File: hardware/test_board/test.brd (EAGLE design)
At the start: 70.5 x 75.9 mm, 25 parts, among them IC2 MAX707CPA, IC3 74HCT573N, IC5 7805DT, J2 POWER_JACKSLT

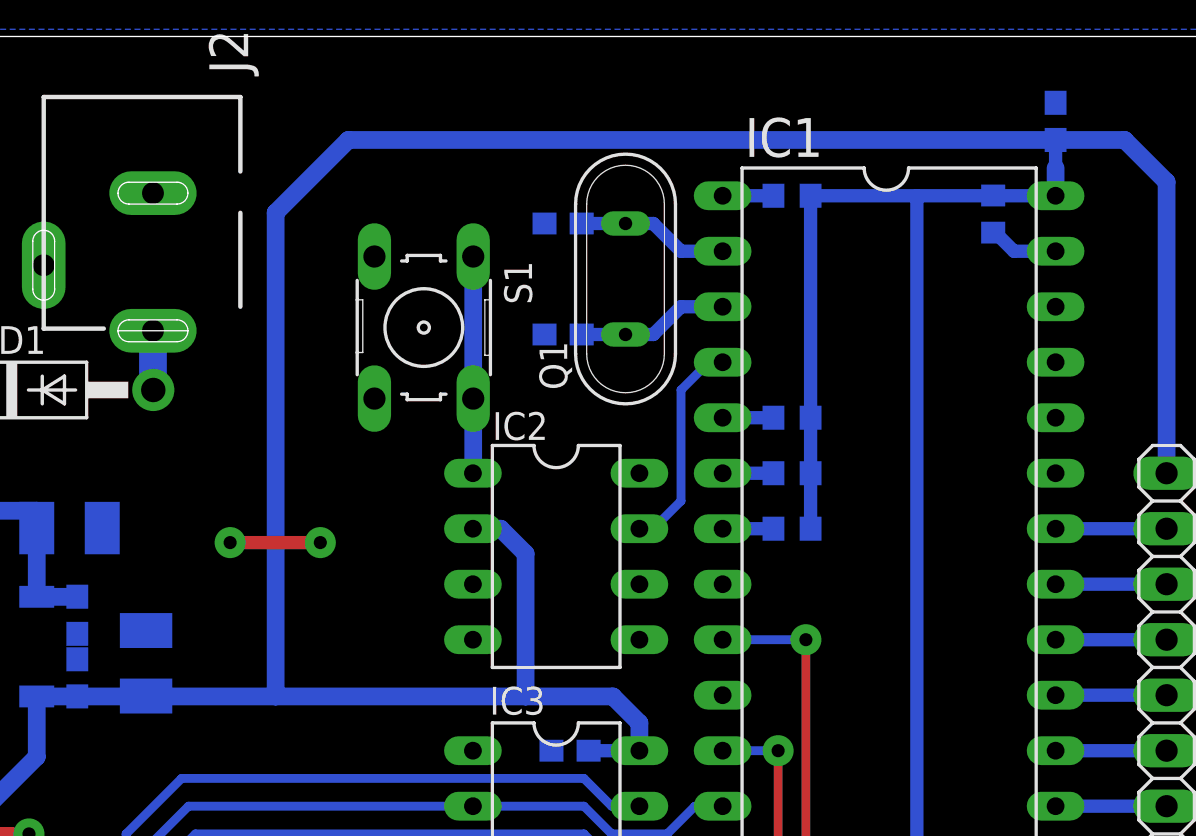
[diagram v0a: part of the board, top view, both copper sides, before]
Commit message: RST circuit simplified according to datasheet
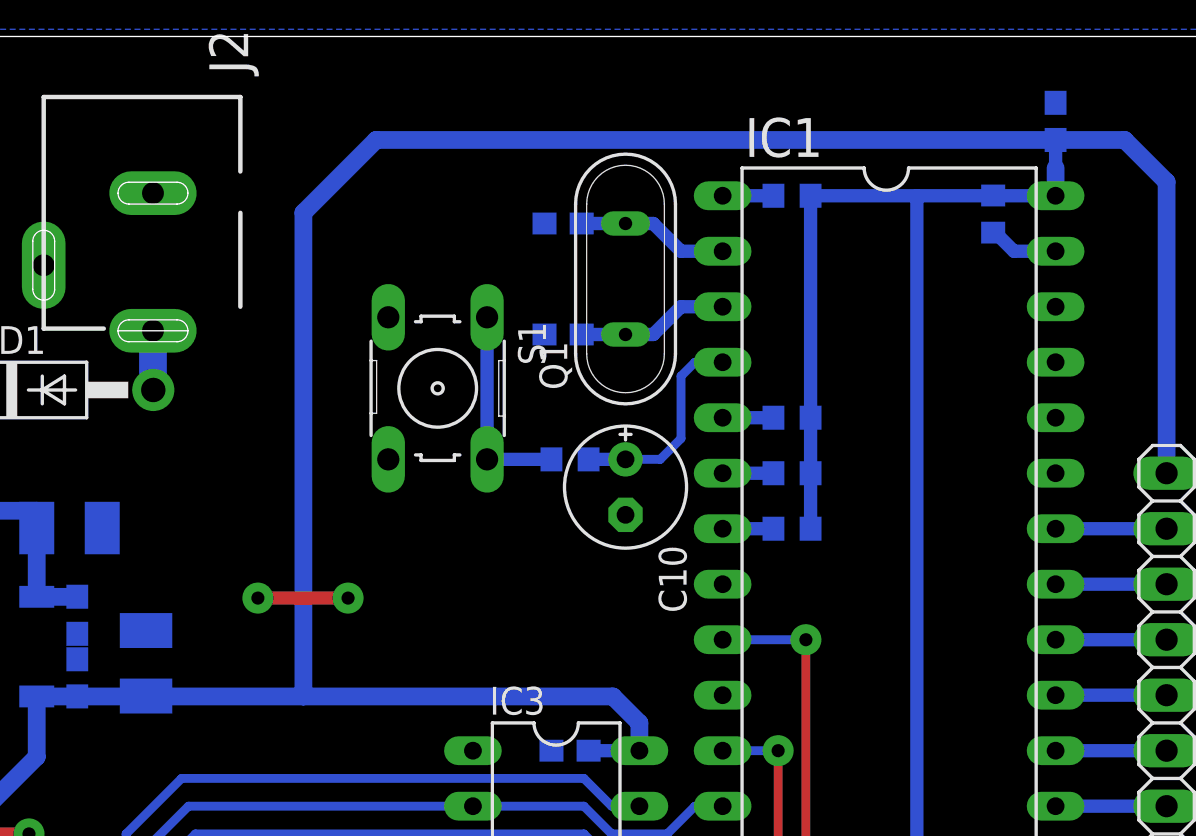
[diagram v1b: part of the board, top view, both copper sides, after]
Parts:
- removed IC2: MAX707CPA, maxim:DIL08
- added C10: (no value), rcl:E2,5-6E
- added R6: (no value), rcl:R0603
- moved S1 2.85 mm to (32.7, 59.8)
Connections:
- net !RESET: now also C10.+, R6.2; no longer IC2.7
- net GND: now also C10.-; no longer IC2.3, IC2.4
- net N$8: now also R6.1; no longer IC2.1
- net VCC: no longer IC2.2
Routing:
- net VCC: track 242.4 -> 231.7 mm
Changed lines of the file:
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@@
 <element name="C3" library="rcl" package="C0603" value="" x="13.97" y="5.08" rot="MR180"/>
 <element name="C4" library="rcl" package="C0603" value="" x="38.735" y="43.18" rot="MR0"/>
-<element name="IC2" library="maxim" package="DIL08" value="MAX707CPA" x="38.1" y="52.07" rot="R270">
-<attribute name="OC_NEWARK" value="34C4006" x="38.1" y="52.07" size="1.778" layer="27" rot="R270" display="off"/>
-<attribute name="MPN" value="MAX707CPA" x="38.1" y="52.07" size="1.778" layer="27" rot="R270" display="off"/>
-<attribute name="MF" value="" x="38.1" y="52.07" size="1.778" layer="27" rot="R270" display="off"/>
-<attribute name="OC_FARNELL" value="1188005" x="38.1" y="52.07" size="1.778" layer="27" rot="R270" display="off"/>
-</element>
-<element name="S1" library="switch-omron" package="B3F-10XX" value="" x="32.0421" y="62.5475" rot="R270">
-<attribute name="OC_NEWARK" value="36M3542" x="32.0421" y="62.5475" size="1.778" layer="27" rot="R270" display="off"/>
-<attribute name="MPN" value="B3F-1000" x="32.0421" y="62.5475" size="1.778" layer="27" rot="R270" display="off"/>
-<attribute name="MF" value="" x="32.0421" y="62.5475" size="1.778" layer="27" rot="R270" display="off"/>
-<attribute name="OC_FARNELL" value="176432" x="32.0421" y="62.5475" size="1.778" layer="27" rot="R270" display="off"/>
+<element name="S1" library="switch-omron" package="B3F-10XX" value="" x="32.6771" y="59.7662" rot="R270">
+<attribute name="OC_NEWARK" value="36M3542" x="32.6771" y="59.7662" size="1.778" layer="27" rot="R270" display="off"/>
+<attribute name="MPN" value="B3F-1000" x="32.6771" y="59.7662" size="1.778" layer="27" rot="R270" display="off"/>
+<attribute name="MF" value="" x="32.6771" y="59.7662" size="1.778" layer="27" rot="R270" display="off"/>
+<attribute name="OC_FARNELL" value="176432" x="32.6771" y="59.7662" size="1.778" layer="27" rot="R270" display="off"/>
 </element>
 <element name="JP1" library="pinhead" package="1X10" value="" x="66.04" y="44.45" rot="R90"/>
@@
 <element name="C8" library="rcl" package="SMC_B" value="" x="19.3294" y="47.1805" rot="MR90"/>
 <element name="C9" library="rcl" package="C0603" value="" x="60.96" y="71.9836" rot="MR90"/>
+<element name="R6" library="rcl" package="R0603" value="" x="38.735" y="56.515" rot="MR180"/>
+<element name="C10" library="rcl" package="E2,5-6E" value="" x="41.275" y="55.245" rot="R270"/>
 </elements>
 <signals>
@@
 <wire x1="13.12" y1="5.08" x2="10.795" y2="5.08" width="0.6096" layer="16"/>
 <wire x1="39.585" y1="43.18" x2="41.91" y2="43.18" width="0.6096" layer="16"/>
-<contactref element="IC2" pad="2"/>
 <contactref element="IC5" pad="2"/>
 <wire x1="14.325" y1="45.6625" x2="15.875" y2="45.6625" width="0.8128" layer="16"/>
 <wire x1="15.875" y1="45.6625" x2="19.05" y2="45.6625" width="0.8128" layer="16"/>
-<wire x1="19.05" y1="45.6625" x2="25.260234375" y2="45.6625" width="0.8128" layer="16"/>
-<wire x1="25.260234375" y1="45.6625" x2="36.700703125" y2="45.6625" width="0.8128" layer="16"/>
-<wire x1="36.700703125" y1="45.6625" x2="40.6975" y2="45.6625" width="0.8128" layer="16"/>
+<wire x1="19.05" y1="45.6625" x2="26.530234375" y2="45.6625" width="0.8128" layer="16"/>
+<wire x1="26.530234375" y1="45.6625" x2="40.6975" y2="45.6625" width="0.8128" layer="16"/>
 <wire x1="40.6975" y1="45.6625" x2="41.91" y2="44.45" width="0.8128" layer="16"/>
 <wire x1="41.91" y1="43.18" x2="41.91" y2="44.45" width="0.8128" layer="16"/>
-<wire x1="36.700703125" y1="45.6625" x2="36.700703125" y2="52.199296875" width="0.8128" layer="16"/>
-<wire x1="36.700703125" y1="52.199296875" x2="35.56" y2="53.34" width="0.8128" layer="16"/>
-<wire x1="35.56" y1="53.34" x2="34.29" y2="53.34" width="0.8128" layer="16"/>
 <wire x1="14.325" y1="45.6625" x2="14.325" y2="42.9" width="0.8128" layer="16"/>
 <wire x1="14.325" y1="42.9" x2="6.35" y2="34.925" width="0.8128" layer="16"/>
@@
 <wire x1="8.89" y1="5.08" x2="10.795" y2="5.08" width="0.8128" layer="16"/>
 <wire x1="10.795" y1="12.7" x2="6.35" y2="12.7" width="0.8128" layer="16"/>
-<wire x1="25.260234375" y1="45.6625" x2="25.260234375" y2="67.805234375" width="0.8128" layer="16"/>
+<wire x1="26.530234375" y1="45.6625" x2="26.530234375" y2="67.805234375" width="0.8128" layer="16"/>
 <wire x1="60.96" y1="69.85" x2="60.96" y2="68.58" width="0.8128" layer="16"/>
 <wire x1="54.61" y1="68.58" x2="54.61" y2="37.465" width="0.6096" layer="16"/>
@@
 <contactref element="C9" pad="1"/>
 <wire x1="59.055" y1="33.02" x2="60.96" y2="33.02" width="0.6096" layer="16"/>
-<wire x1="60.96" y1="71.1336" x2="28.5886" y2="71.1336" width="0.8128" layer="16"/>
-<wire x1="28.5886" y1="71.1336" x2="25.260234375" y2="67.805234375" width="0.8128" layer="16"/>
+<wire x1="60.96" y1="71.1336" x2="29.8586" y2="71.1336" width="0.8128" layer="16"/>
+<wire x1="29.8586" y1="71.1336" x2="26.530234375" y2="67.805234375" width="0.8128" layer="16"/>
 <wire x1="60.96" y1="69.85" x2="60.96" y2="71.1336" width="0.6096" layer="16"/>
 <contactref element="JP1" pad="10"/>
@@
 <contactref element="C3" pad="2"/>
 <contactref element="C4" pad="2"/>
-<contactref element="IC2" pad="3"/>
-<contactref element="IC2" pad="4"/>
 <contactref element="S1" pad="3"/>
 <contactref element="S1" pad="4"/>
@@
 <via x="13.97" y="39.37" extent="1-16" drill="0.6" diameter="1.4224" shape="octagon"/>
 <wire x1="6.985" y1="39.37" x2="13.97" y2="39.37" width="0.6096" layer="1"/>
-<via x="23.1775" y="52.705" extent="1-16" drill="0.6" diameter="1.4224" shape="octagon"/>
-<via x="27.305" y="52.705" extent="1-16" drill="0.6" diameter="1.4224" shape="octagon"/>
-<wire x1="23.1775" y1="52.705" x2="27.305" y2="52.705" width="0.6096" layer="1"/>
+<via x="24.4475" y="50.165" extent="1-16" drill="0.6" diameter="1.4224" shape="octagon"/>
+<via x="28.575" y="50.165" extent="1-16" drill="0.6" diameter="1.4224" shape="octagon"/>
+<wire x1="24.4475" y1="50.165" x2="28.575" y2="50.165" width="0.6096" layer="1"/>
 <via x="52.07" y="20.955" extent="1-16" drill="0.6" diameter="1.4224" shape="octagon"/>
 <via x="52.07" y="13.6525" extent="1-16" drill="0.6" diameter="1.4224" shape="octagon"/>
 <wire x1="52.07" y1="20.955" x2="52.07" y2="13.6525" width="0.6096" layer="1"/>
+<contactref element="C10" pad="-"/>
 </signal>
 <signal name="D0">
@@
 </signal>
 <signal name="!RESET">
-<contactref element="IC2" pad="7"/>
 <contactref element="IC1" pad="4"/>
-<wire x1="41.91" y1="53.34" x2="42.545" y2="53.34" width="0.4064" layer="16"/>
-<wire x1="42.545" y1="53.34" x2="43.815" y2="54.61" width="0.4064" layer="16"/>
-<wire x1="43.815" y1="54.61" x2="43.815" y2="59.69" width="0.4064" layer="16"/>
-<wire x1="43.815" y1="59.69" x2="45.085" y2="60.96" width="0.4064" layer="16"/>
-<wire x1="45.085" y1="60.96" x2="45.72" y2="60.96" width="0.4064" layer="16"/>
-</signal>
-<signal name="N$8">
-<contactref element="IC2" pad="1"/>
-<contactref element="S1" pad="1"/>
-<contactref element="S1" pad="2"/>
-<wire x1="34.3027" y1="65.7987" x2="34.3027" y2="59.2963" width="0.8128" layer="16"/>
-<wire x1="34.3027" y1="59.2963" x2="34.3027" y2="55.8927" width="0.8128" layer="16"/>
-<wire x1="34.3027" y1="55.8927" x2="34.29" y2="55.88" width="0.6096" layer="16"/>
+<wire x1="43.815" y1="57.4675" x2="43.815" y2="60.325" width="0.4064" layer="16"/>
+<wire x1="43.815" y1="60.325" x2="44.45" y2="60.96" width="0.4064" layer="16"/>
+<wire x1="44.45" y1="60.96" x2="45.72" y2="60.96" width="0.4064" layer="16"/>
+<contactref element="R6" pad="2"/>
+<contactref element="C10" pad="+"/>
+<wire x1="41.275" y1="56.515" x2="42.8625" y2="56.515" width="0.4064" layer="16"/>
+<wire x1="42.8625" y1="56.515" x2="43.815" y2="57.4675" width="0.4064" layer="16"/>
+<wire x1="39.585" y1="56.515" x2="41.275" y2="56.515" width="0.6096" layer="16"/>
 </signal>
 <signal name="N$9">
@@
 <wire x1="9.4996" y1="56.9625" x2="9.4996" y2="59.69" width="0.8128" layer="16"/>
 </signal>
+<signal name="N$8">
+<contactref element="S1" pad="1"/>
+<contactref element="S1" pad="2"/>
+<contactref element="R6" pad="1"/>
+<wire x1="37.885" y1="56.515" x2="34.9377" y2="56.515" width="0.6096" layer="16"/>
+<wire x1="34.9377" y1="56.515" x2="34.9377" y2="63.0174" width="0.6096" layer="16"/>
+</signal>
 </signals>

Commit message: Minor optimizations
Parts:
- removed JP1: (no value), pinhead:1X10
- added C11: (no value), rcl:C0603
- added JP2: (no value), pinhead:1X15
- R1, R2, R3, R5: device rcl:R0603 -> rcl:R1206
- moved R1 1.27 mm to (50.2, 58.4)
- moved R2 1.27 mm to (50.2, 53.3)
- moved R3 1.27 mm to (50.2, 68.6)
- moved R5 1.27 mm to (50.2, 55.9)
- renumbered IC4 to IC2
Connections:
- removed net N$7: IC1.6, R5.1
- new net A11: IC1.24, IC2.21
- new net INT: IC1.6, JP2.14, R5.1
- new net N$17: IC1.35, JP2.10
- new net N$19: IC1.36, JP2.11
- new net N$21: IC1.37, JP2.12
- new net N$22: IC1.38, JP2.13
- net GND: now also C11.2, JP2.1; no longer IC2.18, JP1.1
- net N$10: now also JP2.3; no longer JP1.3
- net N$11: now also JP2.4; no longer JP1.4
- net N$12: now also JP2.5; no longer JP1.5
- net N$13: now also JP2.6; no longer JP1.6
- net N$14: now also JP2.7; no longer JP1.7
- net N$15: now also JP2.8; no longer JP1.8
- net N$16: now also JP2.9; no longer JP1.9
- net N$9: now also JP2.2; no longer JP1.2
- net VCC: now also C11.1, JP2.15; no longer IC2.21, JP1.10
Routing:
- net A11: track 0.00 -> 56.5 mm
- net INT: track 0.00 -> 27.9 mm, vias 0 -> 2
- net VCC: track 231.7 -> 207.0 mm
- net A10: track 53.3 -> 65.4 mm
- net GND: track 27.9 -> 37.5 mm
- net N$22: track 0.00 -> 5.08 mm
- net N$21: track 0.00 -> 5.08 mm
- net N$19: track 0.00 -> 5.08 mm
- net N$17: track 0.00 -> 5.08 mm
- net EPROM_OE: track 74.1 -> 71.0 mm
- net ALE: track 31.0 -> 33.5 mm
- net N$7: track 2.33 -> 0.00 mm
- net A5: track 32.5 -> 33.6 mm
- net A9: track 55.4 -> 56.5 mm
- net A8: track 55.4 -> 56.5 mm
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
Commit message: Few more optimizations
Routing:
- net GND: track 37.5 -> 15.6 mm, vias 8 -> 6
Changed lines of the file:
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@@
 <setting verticaltext="up"/>
 </settings>
-<grid distance="25" unitdist="mil" unit="mil" style="lines" multiple="1" display="no" altdistance="1" altunitdist="mil" altunit="mil"/>
+<grid distance="25" unitdist="mil" unit="mil" style="lines" multiple="1" display="no" altdistance="12.5" altunitdist="mil" altunit="mil"/>
 <layers>
 <layer number="1" name="Top" color="4" fill="1" visible="yes" active="yes"/>
@@
 <vertex x="70.485" y="76.2"/>
 </polygon>
-<via x="38.735" y="20.955" extent="1-16" drill="0.6" diameter="1.4224" shape="octagon"/>
-<via x="38.735" y="8.89" extent="1-16" drill="0.6" diameter="1.4224" shape="octagon"/>
-<wire x1="38.735" y1="20.955" x2="38.735" y2="8.89" width="0.6096" layer="1"/>
+<via x="44.45" y="18.415" extent="1-16" drill="0.6" diameter="1.4224" shape="octagon"/>
+<via x="44.45" y="10.795" extent="1-16" drill="0.6" diameter="1.4224" shape="octagon"/>
+<wire x1="44.45" y1="18.415" x2="44.45" y2="10.795" width="0.6096" layer="1"/>
 <contactref element="IC3" pad="1"/>
 <contactref element="C1" pad="2"/>
@@
 <contactref element="C8" pad="-"/>
 <contactref element="C9" pad="2"/>
-<via x="6.985" y="39.37" extent="1-16" drill="0.6" diameter="1.4224" shape="octagon"/>
-<via x="13.97" y="39.37" extent="1-16" drill="0.6" diameter="1.4224" shape="octagon"/>
-<wire x1="6.985" y1="39.37" x2="13.97" y2="39.37" width="0.6096" layer="1"/>
+<via x="24.4475" y="47.625" extent="1-16" drill="0.6" diameter="1.4224" shape="octagon"/>
+<via x="24.4475" y="43.815" extent="1-16" drill="0.6" diameter="1.4224" shape="octagon"/>
+<wire x1="24.4475" y1="47.625" x2="24.4475" y2="43.815" width="0.6096" layer="1"/>
 <via x="24.4475" y="50.165" extent="1-16" drill="0.6" diameter="1.4224" shape="octagon"/>
 <via x="28.575" y="50.165" extent="1-16" drill="0.6" diameter="1.4224" shape="octagon"/>
 <wire x1="24.4475" y1="50.165" x2="28.575" y2="50.165" width="0.6096" layer="1"/>
-<via x="53.975" y="25.4" extent="1-16" drill="0.6" diameter="1.4224" shape="octagon"/>
-<via x="53.975" y="11.1125" extent="1-16" drill="0.6" diameter="1.4224" shape="octagon"/>
-<wire x1="53.975" y1="25.4" x2="53.975" y2="11.1125" width="0.6096" layer="1"/>
 <contactref element="C10" pad="-"/>
 <contactref element="JP2" pad="1"/>

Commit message: Code examples and fix of bug in PCB design
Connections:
- net GND: now also IC2.18
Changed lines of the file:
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@@
 <contactref element="IC2" pad="12"/>
 <contactref element="C11" pad="2"/>
+<contactref element="IC2" pad="18"/>
 </signal>
 <signal name="D0">
